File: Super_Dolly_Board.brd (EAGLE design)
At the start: 154.5 x 44.5 mm, 94 parts, among them J1 10118193-0001LF, J3 SJ1-2503A, J4 RJHSE-5381, J5 SJ1-2503A, J6 SJ1-2503A, P1 TC33X-2, SW1 SKQUDBE010, U1 AT90USB646-MU, U10 IP4234CZ6, U11 AT90USB646-AU, U2 MMDT3904, U3 TB6559FG, U4 TS2937CW50, U5 TB6559FG, U6 SN75176BDR, U7 TB6559FG, U8 TPD2E007DCK, U9 TS2937CW50, X1 3.2X2.5MMCRYSTAL

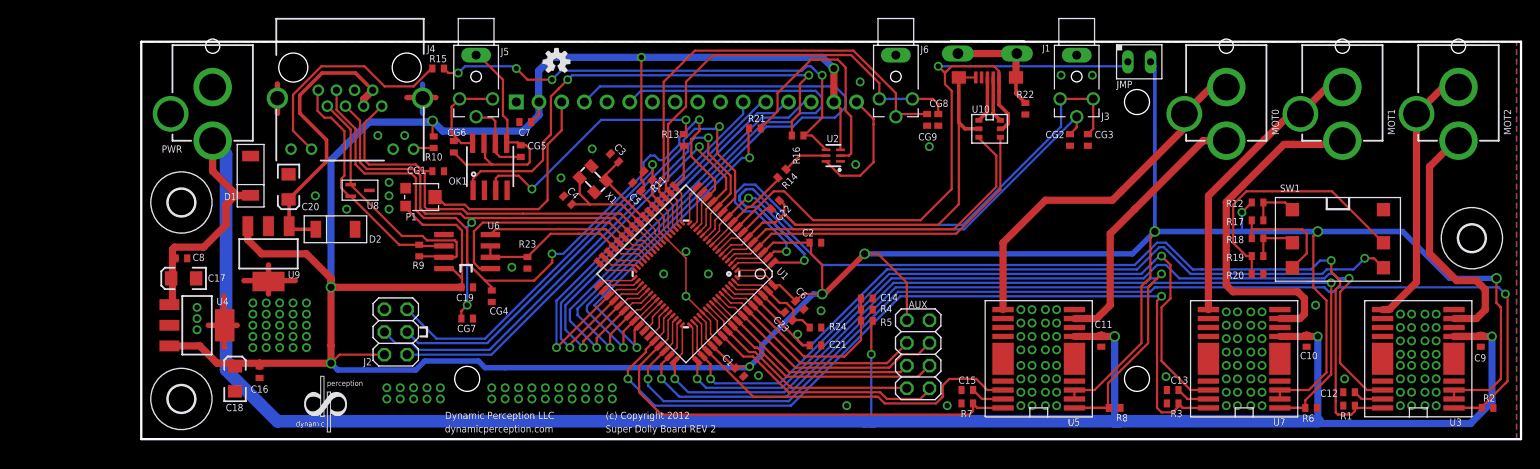
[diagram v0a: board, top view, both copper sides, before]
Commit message: REV 3 of SDB in works. Fixed the pull up on the BTNS, changes RS485 chip to one with ESD built in.
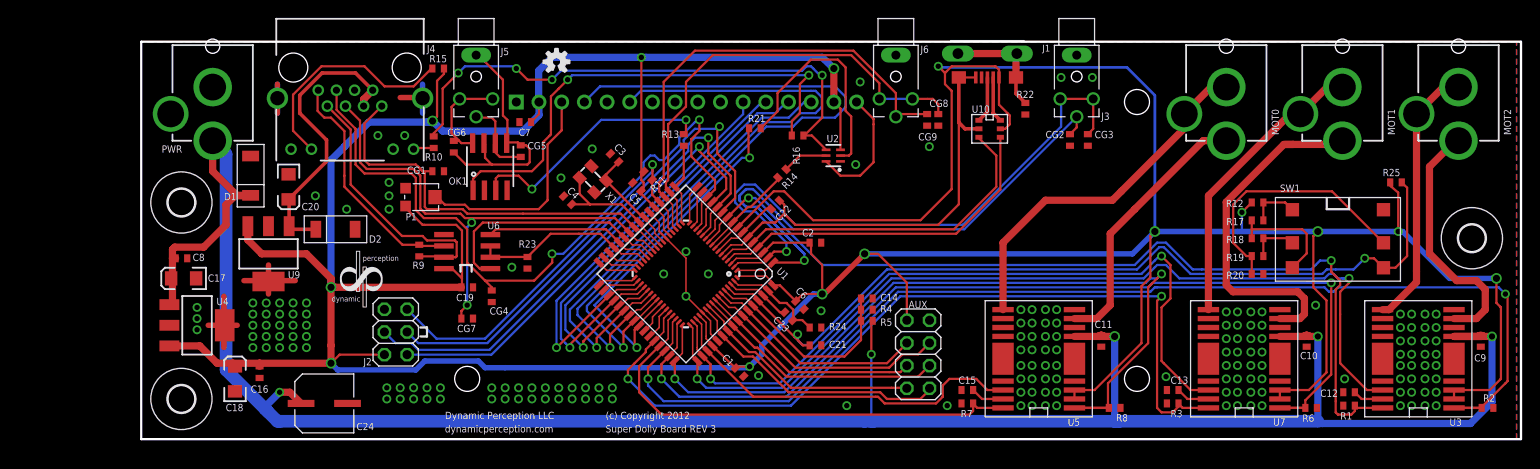
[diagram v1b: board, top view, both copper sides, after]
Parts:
- removed JMP: P1X02PH, parkers_parts:P1X02
- removed U8: TPD2E007DCK, parkers_parts:DCK
- added C24: 100uF, PP_Passives:6.3MM_CAP_SMD
- added R25: 10K, parkers_parts:0402_RES
- R13: value 68 -> 100
- R16: value 43 -> 100
- U6: value SN75176BDR -> ISL8483
- moved LOGO2 14.6 mm to (-51.8, -10.8)
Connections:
- removed net VUSB: J1.1, JMP.1, U1.8, U10.5, U11.8
- net +5V: now also J1.1, R15.1, R25.1, U1.8, U10.5, U11.8; no longer JMP.2, R10.2
- net A: no longer U8.2
- net B: no longer U8.1
- net BTNS: now also R25.2
- net GND: now also C24.NEG; no longer U8.3
- net OK_SHT: now also R10.2; no longer R15.1
- net VIN: now also C24.POS
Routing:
- net +5V: track 479.5 -> 572.9 mm, vias 12 -> 14
- net VUSB: track 83.4 -> 0.00 mm, vias 1 -> 0
- net BTNS: track 85.9 -> 97.6 mm
- net VIN: track 255.0 -> 262.3 mm, vias 4 -> 5
- net OK_SHT: track 55.4 -> 61.8 mm
- net A: track 27.0 -> 26.4 mm
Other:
- board text added: "Super Dolly Board REV 3"
- board text removed: "Super Dolly Board REV 2"

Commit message: REV 7 of the USB Board done. Moving to production on it.
SDB Rev 3 almost done. OTG USB added. Motor controllers switched to BTM7755 to reduce the Resistance on of the drivers.
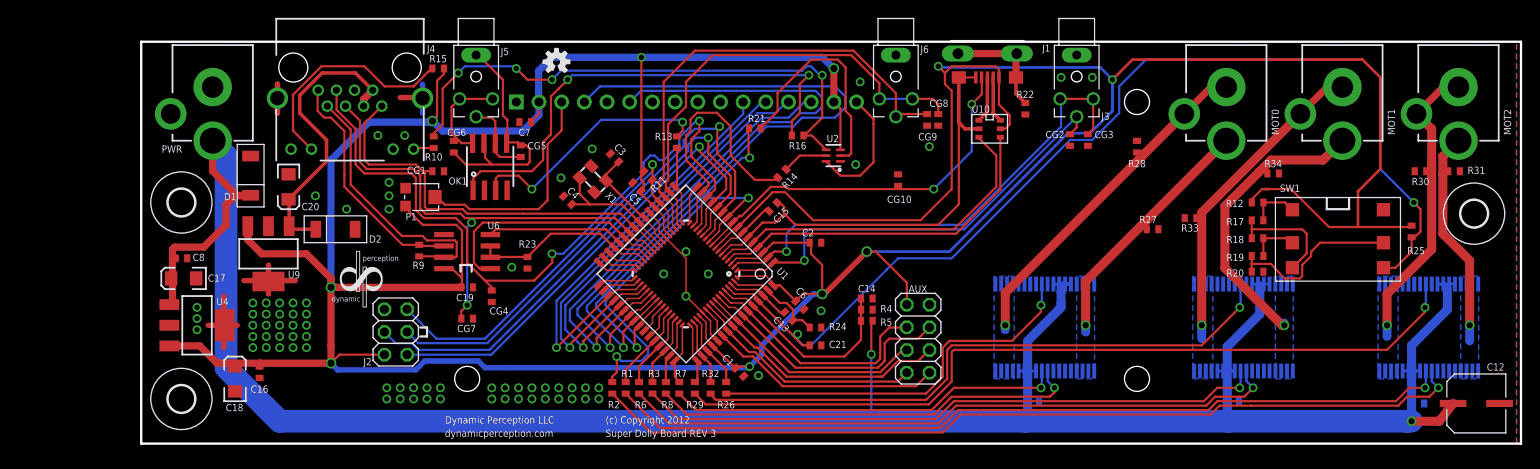
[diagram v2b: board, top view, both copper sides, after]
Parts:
- removed C22: 1uF, parkers_parts:0402_CAP
- removed C23: .1uF, parkers_parts:0402_CAP
- removed C24: 100uF, PP_Passives:6.3MM_CAP_SMD
- added CG10: CG0402MLC-05LG, parkers_parts:0402_RES
- added R26, R29: 4.7K, parkers_parts:0402_RES
- added R27, R28, R30, R31, R32, R33, R34: 10K, parkers_parts:0402_RES
- C12: value .1uF -> 100uF; device parkers_parts:0402_CAP -> PP_Passives:6.3MM_CAP_SMD
- C15: value .1uF -> 1uF
- C9: value .1uF -> .1uF 35V
- MOT0, MOT1, MOT2, PWR: device parkers_parts:POWER_JACK_PTH -> PP_Connectors:DC_JACK_PTH_TIGHT
- R1, R2, R7, R8: value 10K -> 4.7K
- U3: value TB6559FG -> BTM7755; device parkers_parts:HSOP16 -> PP_PowerIC:PG-DSO-36-29
- U5, U7: value TB6559FG -> (none); device parkers_parts:HSOP16 -> PP_PowerIC:PG-DSO-36-29
- moved R2 98.0 mm to (-21.2, -19.7), turned to 90 degrees
- moved R1 81.0 mm to (-19.8, -19.8), turned to 90 degrees
- moved R6 75.3 mm to (-18.2, -19.7), turned to 90 degrees
- moved R3 58.3 mm to (-16.8, -19.8), turned to 90 degrees
- moved R8 50.3 mm to (-15.2, -19.8), turned to 90 degrees
- moved C13 43.8 mm to (-1.50, -11.8), turned to 315 degrees
- moved R7 32.3 mm to (-13.8, -19.8), turned to 90 degrees
- moved C15 29.9 mm to (-3.25, 0.50), turned to 225 degrees
- moved C12 14.3 mm to (75.5, -21.5), turned to 90 degrees
- moved LOGO1 12.1 mm to (23.5, -7.25)
- moved C10 10.7 mm to (48.2, -21.2), flipped to the bottom, turned to 0 degrees
- moved C11 10.3 mm to (25.9, -21.4), flipped to the bottom, turned to 0 degrees
- moved C9 9.90 mm to (69.0, -21.5), flipped to the bottom, turned to 0 degrees
- moved U3 6.18 mm to (70.5, -13.0), flipped to the bottom, turned to 90 degrees
- moved U5 6.08 mm to (27.5, -13.0), flipped to the bottom, turned to 90 degrees
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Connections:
- removed net N$15: C15.1, U5.15
- removed net N$19: C13.1, U7.15
- removed net N$40: C12.1, U3.15
- removed net PB5: U1.15, U11.15
- new net N$1: R7.1, U5.10
- new net N$10: R1.1, U3.10
- new net N$2: R8.1, U5.9
- new net N$3: R26.1, U5.27
- new net N$4: R3.1, U7.10
- new net N$6: R6.1, U7.9
- new net N$7: R32.1, U7.27
- new net N$8: R29.1, U3.27
- new net N$9: R2.1, U3.9
- new net PE3: CG10.2, U1.9, U11.9
- net +5V: no longer U3.2, U3.3, U5.2, U5.3, U7.2, U7.3
- net AGND: now also C13.2; no longer C23.2
- net AREF: now also C13.1; no longer C23.1
- net GND: now also C10.1, C11.1, C12.NEG, C9.1, CG10.1, R27.2, R28.2, R30.2, R31.2, R33.2, R34.2, U3.23, U3.24, U3.25, U3.26, U3.5, U3.6, U3.7, U5.23, U5.24, U5.25, U5.26, U5.5, U5.6, U5.7, U7.23, U7.24, U7.25, U7.26, U7.5, U7.6, U7.7; no longer C10.2, C11.2, C12.2, C13.2, C15.2, C24.NEG, C9.2, R1.1, R2.1, R3.1, R6.1, R7.1, R8.1, U3.10, U3.12, U3.13, U3.4, U3.FIN0, U3.FIN1, U5.10, U5.12, U5.13, U5.4, U5.FIN0, U5.FIN1, U7.10, U7.12, U7.13, U7.4, U7.FIN0, U7.FIN1
- net M0_A: now also R7.2; no longer R8.2, U5.1
- net M0_B: now also R8.2, U1.47, U11.47; no longer R7.2, U1.45, U11.45, U5.16
- net M0_O1: now also R27.1, U5.1, U5.2, U5.3, U5.33, U5.34, U5.35, U5.36, U5.4; no longer U5.7
- net M0_O2: now also R28.1, U5.15, U5.16, U5.17, U5.18, U5.19, U5.20, U5.21, U5.22; no longer U5.9
- net M0_P: now also R26.2; no longer U5.14
- net M1_A: now also R3.2, U1.46, U11.46; no longer R6.2, U1.47, U11.47, U7.1
- net M1_B: now also R6.2, U1.45, U11.45; no longer R3.2, U1.44, U11.44, U7.16
- net M1_O1: now also R34.1, U7.1, U7.2, U7.3, U7.33, U7.34, U7.35, U7.36, U7.4; no longer U7.7
- net M1_O2: now also R33.1, U7.15, U7.16, U7.17, U7.18, U7.19, U7.20, U7.21, U7.22; no longer U7.9
- net M1_P: now also R32.2; no longer U7.14
- net M2_A: now also R1.2, U1.44, U11.44; no longer R2.2, U1.46, U11.46, U3.1
- net M2_B: now also R2.2; no longer R1.2, U3.16
- net M2_O1: now also R31.1, U3.1, U3.2, U3.3, U3.33, U3.34, U3.35, U3.36, U3.4; no longer U3.7
- net M2_O2: now also R30.1, U3.15, U3.16, U3.17, U3.18, U3.19, U3.20, U3.21, U3.22; no longer U3.9
- net M2_P: now also R29.2; no longer U3.14
- net SHT: now also U1.15, U11.15; no longer U1.9, U11.9
- net UCAP: now also C15.2; no longer C22.2
- net UGND: now also C15.1; no longer C22.1
- net VIN: now also C10.2, C11.2, C12.POS, C9.2, U3.11, U3.12, U3.13, U3.14, U3.29, U3.30, U3.31, U3.32, U5.11, U5.12, U5.13, U5.14, U5.29, U5.30, U5.31, U5.32, U7.11, U7.12, U7.13, U7.14, U7.29, U7.30, U7.31, U7.32; no longer C10.1, C11.1, C24.POS, C9.1, U3.5, U5.5, U7.5
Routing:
- net M2_A: track 131.7 -> 9.87 mm, vias 2 -> 0
- net M1_A: track 111.9 -> 8.21 mm, vias 2 -> 0
- net N$9: track 0.00 -> 98.6 mm, vias 0 -> 1
- net M2_P: track 103.2 -> 6.87 mm, vias 2 -> 0
- net N$10: track 0.00 -> 94.9 mm, vias 0 -> 1
- net N$8: track 0.00 -> 91.6 mm, vias 0 -> 1
- net M1_B: track 95.0 -> 9.11 mm, vias 2 -> 0
- net M0_A: track 92.1 -> 6.94 mm, vias 2 -> 0
- net VIN: track 262.3 -> 345.0 mm, vias 5 -> 2
- net M1_P: track 83.0 -> 7.57 mm, vias 2 -> 0
- net N$6: track 0.00 -> 74.0 mm, vias 0 -> 1
- net N$4: track 0.00 -> 70.3 mm, vias 0 -> 1
- net N$7: track 0.00 -> 68.4 mm, vias 0 -> 1
- net M2_B: track 102.0 -> 42.7 mm
- net +5V: track 572.9 -> 514.7 mm, vias 14 -> 10
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- added copper zone on layer 16, net M0_O1
- added copper zone on layer 16, net M0_O2
- added copper zone on layer 16, net M1_O1
- added copper zone on layer 16, net M1_O2
- added copper zone on layer 16, net M2_O1
- added copper zone on layer 16, net M2_O2
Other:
- board size 154.5 x 44.5 mm -> 154.5 x 45 mm

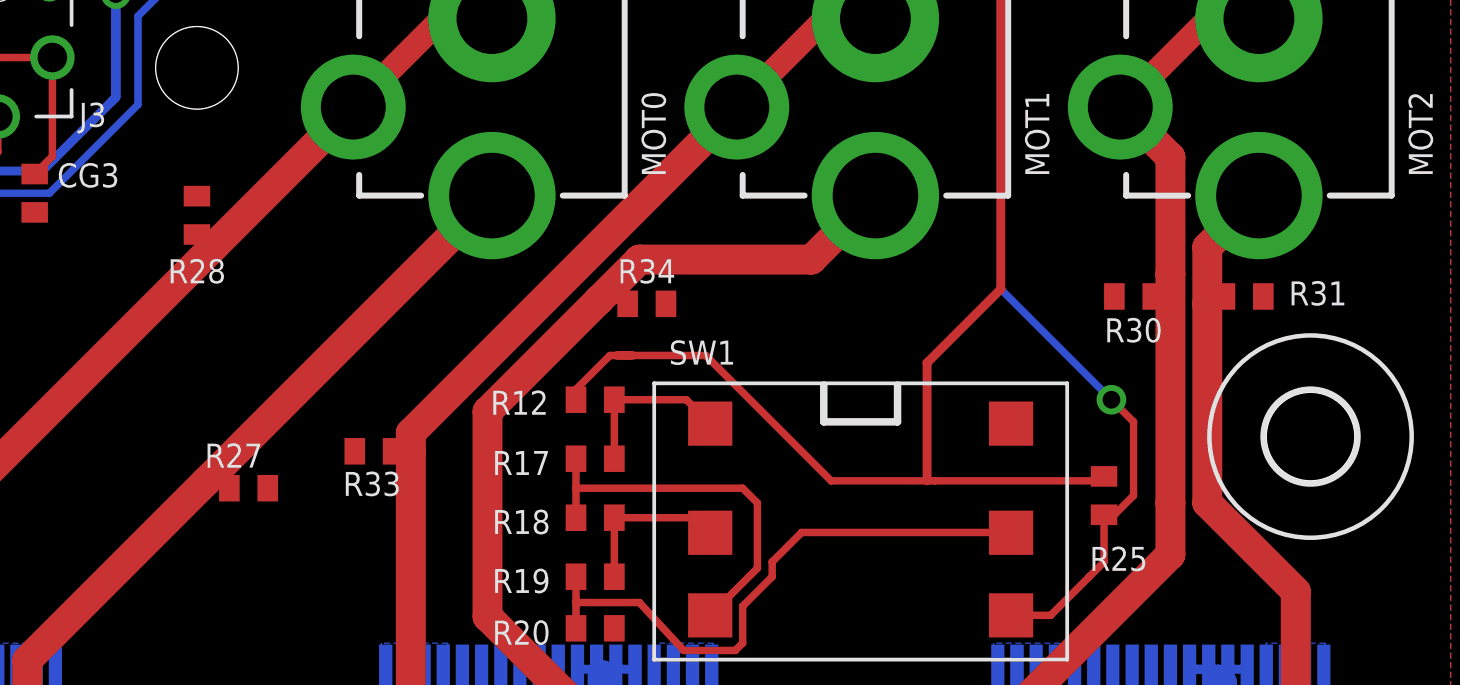
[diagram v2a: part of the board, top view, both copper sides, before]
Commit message: added 0805 package to pp_passives for resistors. changed resistors on the motor output lines from 0402 to 0805 for better heat dissipation.
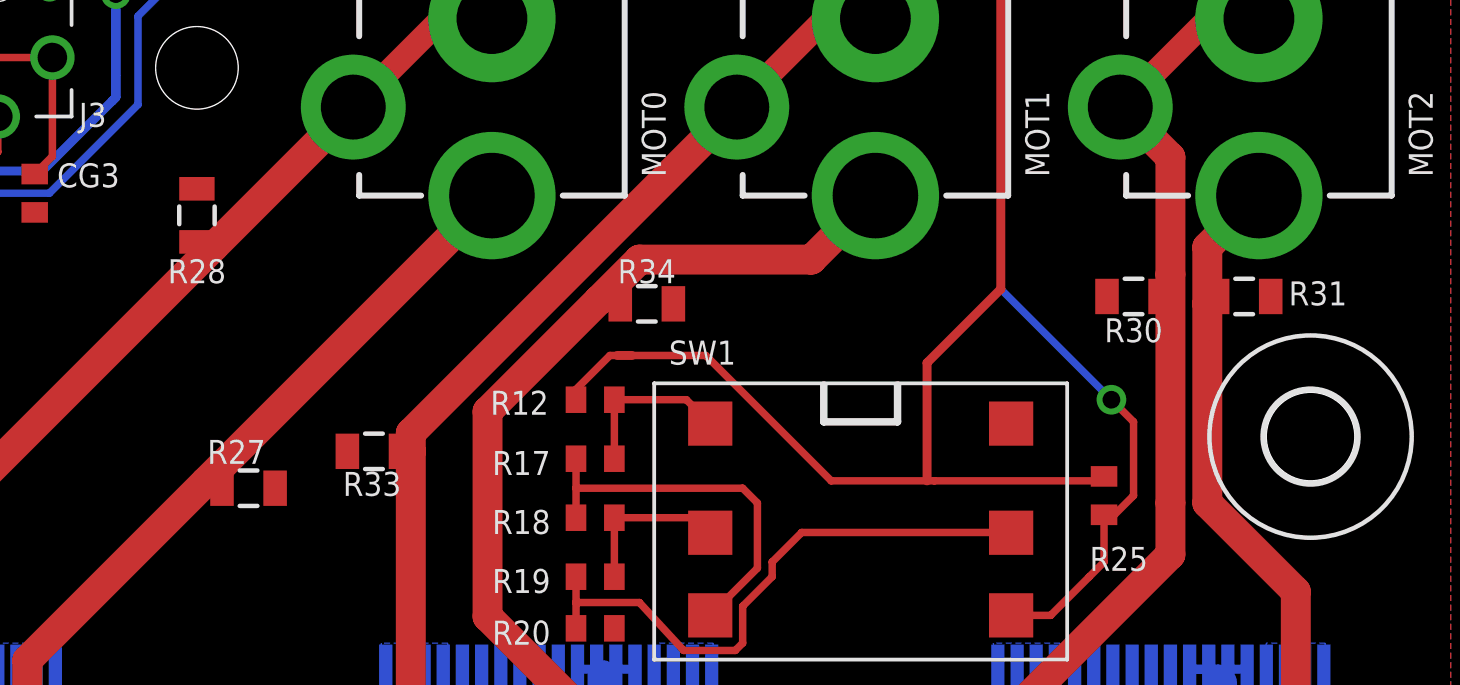
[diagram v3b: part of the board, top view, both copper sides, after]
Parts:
- R27, R28, R30, R31, R33, R34: device parkers_parts:0402_RES -> PP_Passives:0805
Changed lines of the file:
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@@
 <attribute name="NAME" x="-9.489" y="-22.0515" size="0.8128" layer="25" font="vector"/>
 </element>
-<element name="R27" library="parkers_parts" package="0402_RES" value="10K" x="39.250003125" y="-1.999996875"/>
-<element name="R28" library="parkers_parts" package="0402_RES" value="10K" x="37.5" y="7.250003125" smashed="yes" rot="R90">
+<element name="R27" library="PP_Passives" package="0805" value="10K" x="39.250003125" y="-1.999996875"/>
+<element name="R28" library="PP_Passives" package="0805" value="10K" x="37.5" y="7.250003125" smashed="yes" rot="R90">
 <attribute name="NAME" x="36.511003125" y="4.9485" size="0.8128" layer="25" font="vector"/>
 </element>
@@
 <attribute name="NAME" x="-12.988996875" y="-22.0515" size="0.8128" layer="25" font="vector"/>
 </element>
-<element name="R30" library="parkers_parts" package="0402_RES" value="10K" x="69.25" y="4.5" smashed="yes" rot="R180">
+<element name="R30" library="PP_Passives" package="0805" value="10K" x="69.25" y="4.5" smashed="yes" rot="R180">
 <attribute name="NAME" x="68.26100625" y="2.9485" size="0.8128" layer="25" font="vector"/>
 </element>
-<element name="R31" library="parkers_parts" package="0402_RES" value="10K" x="73.00000625" y="4.5" smashed="yes">
+<element name="R31" library="PP_Passives" package="0805" value="10K" x="73.00000625" y="4.5" smashed="yes">
 <attribute name="NAME" x="74.51100625" y="4.1985" size="0.8128" layer="25" font="vector"/>
 </element>
@@
 <attribute name="NAME" x="-11.238996875" y="-18.5515" size="0.8128" layer="25" font="vector"/>
 </element>
-<element name="R33" library="parkers_parts" package="0402_RES" value="10K" x="43.499996875" y="-0.75" smashed="yes" rot="R180">
+<element name="R33" library="PP_Passives" package="0805" value="10K" x="43.499996875" y="-0.75" smashed="yes" rot="R180">
 <attribute name="NAME" x="42.4485" y="-2.261003125" size="0.8128" layer="25" font="vector"/>
 </element>
-<element name="R34" library="parkers_parts" package="0402_RES" value="10K" x="52.75000625" y="4.25" smashed="yes">
+<element name="R34" library="PP_Passives" package="0805" value="10K" x="52.75000625" y="4.25" smashed="yes">
 <attribute name="NAME" x="51.76100625" y="4.9485" size="0.8128" layer="25" font="vector"/>
 </element>
@@
 <via x="74.750003125" y="-12.75" extent="1-16" drill="0.7"/>
 <wire x1="74.750003125" y1="-12.75" x2="74.750003125" y2="-14.5" width="1.016" layer="16"/>
-<wire x1="72.35000625" y1="4.5" x2="72.10000625" y2="4.25" width="0.254" layer="1"/>
+<wire x1="72.10000625" y1="4.5" x2="72.10000625" y2="4.25" width="0.254" layer="1"/>
 <wire x1="72.10000625" y1="4.25" x2="71.750003125" y2="4.25" width="0.254" layer="1"/>
 </signal>
@@
 <via x="54.000003125" y="-12.75" extent="1-16" drill="0.7"/>
 <wire x1="54.000003125" y1="-12.75" x2="54.000003125" y2="-12.5" width="1.016" layer="16"/>
-<wire x1="52.10000625" y1="4.25" x2="51.97500625" y2="4.375" width="0.254" layer="1"/>
+<wire x1="51.85000625" y1="4.25" x2="51.97500625" y2="4.375" width="0.254" layer="1"/>
 <wire x1="51.97500625" y1="4.375" x2="51.125003125" y2="4.375" width="0.254" layer="1"/>
 </signal>
@@
 <via x="31.75" y="-12.75" extent="1-16" drill="0.7"/>
 <wire x1="31.75" y1="-12.75" x2="31.75" y2="-13.5" width="1.016" layer="16"/>
-<wire x1="38.600003125" y1="-1.999996875" x2="38.39000625" y2="-1.79" width="0.254" layer="1"/>
+<wire x1="38.350003125" y1="-1.999996875" x2="38.39000625" y2="-1.79" width="0.254" layer="1"/>
 <wire x1="38.39000625" y1="-1.79" x2="37.79" y2="-1.79" width="0.254" layer="1"/>
 </signal>
@@
 <via x="22.75" y="-12.75" extent="1-16" drill="0.7"/>
 <wire x1="22.75" y1="-12.75" x2="22.75" y2="-13.25" width="1.016" layer="16"/>
-<wire x1="37.5" y1="6.600003125" x2="37.915003125" y2="6.185" width="0.254" layer="1"/>
+<wire x1="37.5" y1="6.350003125" x2="37.915003125" y2="6.185" width="0.254" layer="1"/>
 <wire x1="37.915003125" y1="6.185" x2="38.065" y2="6.185" width="0.254" layer="1"/>
 </signal>
@@
 <via x="65.500003125" y="-12.75" extent="1-16" drill="0.7"/>
 <wire x1="65.500003125" y1="-12.75" x2="65.500003125" y2="-14" width="1.016" layer="16"/>
-<wire x1="69.9" y1="4.5" x2="70.500003125" y2="5.100003125" width="0.254" layer="1"/>
+<wire x1="70.15" y1="4.5" x2="70.500003125" y2="5.100003125" width="0.254" layer="1"/>
 <wire x1="70.500003125" y1="5.100003125" x2="70.500003125" y2="5.25" width="0.254" layer="1"/>
 </signal>
@@
 <wire x1="44.75" y1="-0.75" x2="44.75" y2="-12.75" width="1.016" layer="1"/>
 <wire x1="44.75" y1="-12.75" x2="44.75" y2="-14.25" width="1.016" layer="16"/>
-<wire x1="44.149996875" y1="-0.75" x2="44.75" y2="-0.75" width="0.254" layer="1"/>
+<wire x1="44.399996875" y1="-0.75" x2="44.75" y2="-0.75" width="0.254" layer="1"/>
 </signal>
 <signal name="M2_P">
@@
 </signal>
 </signals>
-<errors>
-</errors>
 </board>
 </drawing>

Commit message: updated cam files for trunk (REV3) of the Super Dolly Board
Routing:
- net OK_SHT: track 61.8 -> 63.9 mm
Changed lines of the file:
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@@
 <wire x1="-30.75" y1="14.75" x2="-32" y2="16" width="0.254" layer="1"/>
 <via x="-32" y="16" extent="1-16" drill="0.6"/>
-<wire x1="-32" y1="16" x2="-32.25" y2="16.25" width="0.254" layer="16"/>
-<wire x1="-32.25" y1="16.25" x2="-37.75" y2="16.25" width="0.254" layer="16"/>
-<wire x1="-37.75" y1="16.25" x2="-38.5" y2="15.5" width="0.254" layer="16"/>
 <via x="-38.5" y="15.5" extent="1-16" drill="0.6"/>
 <contactref element="R10" pad="2"/>
@@
 <wire x1="-40.25" y1="9.75" x2="-41.25" y2="8.75" width="0.254" layer="1"/>
 <wire x1="-41.25" y1="8.75" x2="-41.25" y2="8.4" width="0.254" layer="1"/>
+<wire x1="-38.5" y1="15.5" x2="-38.5" y2="14.75" width="0.254" layer="16"/>
+<wire x1="-38.5" y1="14.75" x2="-37.5" y2="13.75" width="0.254" layer="16"/>
+<wire x1="-37.5" y1="13.75" x2="-37" y2="13.25" width="0.254" layer="16"/>
+<wire x1="-37" y1="13.25" x2="-35.75" y2="13.25" width="0.254" layer="16"/>
+<wire x1="-35.75" y1="13.25" x2="-35.25" y2="13.75" width="0.254" layer="16"/>
+<wire x1="-35.25" y1="13.75" x2="-33" y2="16" width="0.254" layer="16"/>
+<wire x1="-33" y1="16" x2="-32" y2="16" width="0.254" layer="16"/>
 </signal>
 <signal name="CAM_SHT">
